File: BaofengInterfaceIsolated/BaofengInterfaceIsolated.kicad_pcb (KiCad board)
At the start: 2 copper layers, 39.4 x 50.8 mm, 11 parts, among them J1 CONN_01X06, J2 CONN_01X02, J3 JACK_TRS_3PINS, J4 JACK_TRS_3PINS, J5 CONN_01X03, J6 CONN_02X04, J7 CONN_01X02, T1 LM-NP-1001-B1L, T2 LM-NP-1001-B1L, U1 LTV-817

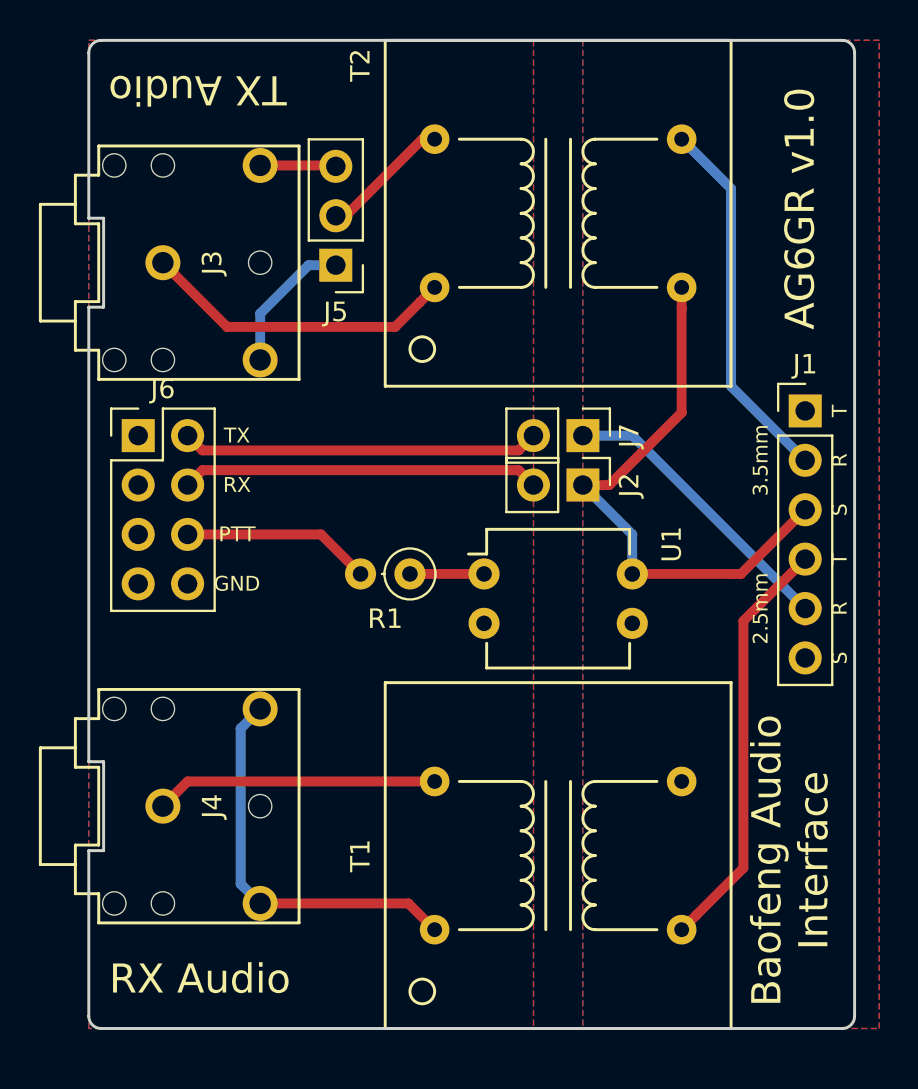
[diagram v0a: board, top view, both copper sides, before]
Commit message: Cleanup board edge, silkscreen
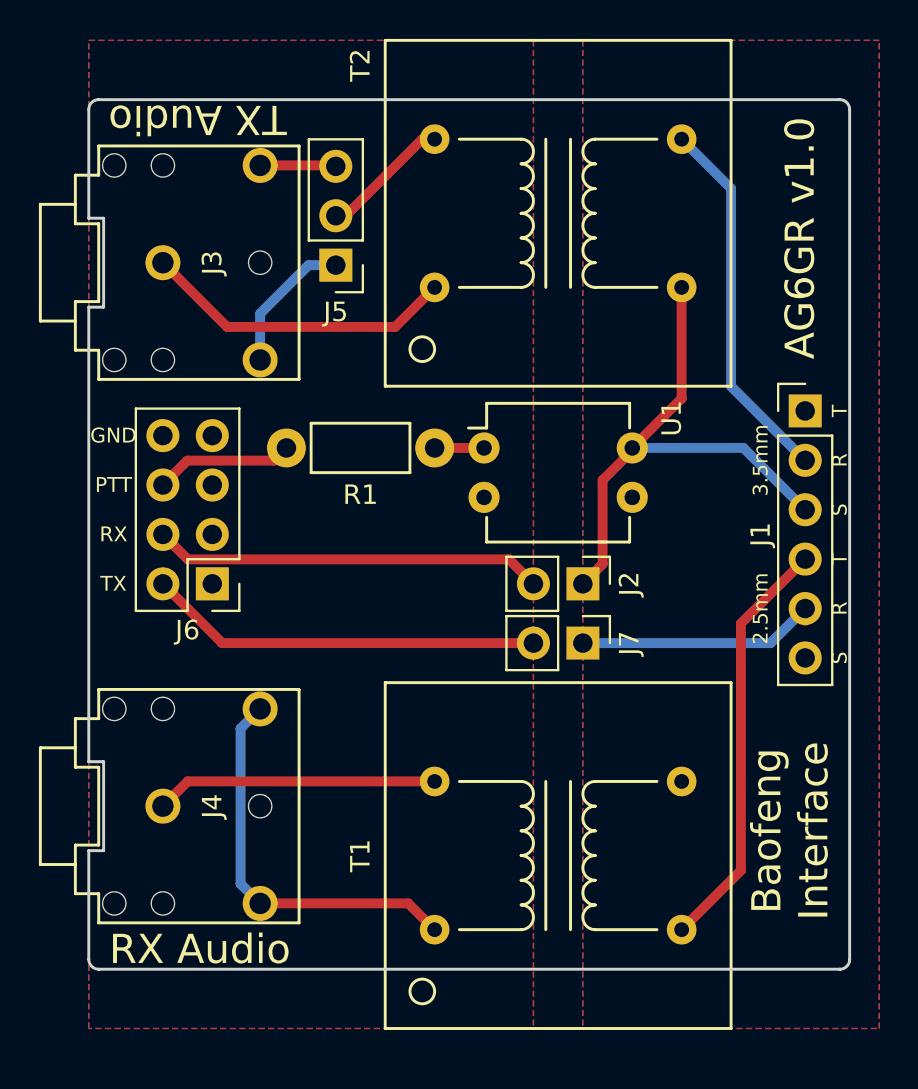
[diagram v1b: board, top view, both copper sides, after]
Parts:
- R1: footprint Resistors_THT:R_Axial_DIN0207_L6.3mm_D2.5mm_P2.54mm_Vertical -> Resistors_THT:Resistor_Horizontal_RM7mm
- moved J7 10.7 mm to (127.0, 132.6)
- moved J6 8.52 mm to (108.0, 129.5), turned to 180 degrees
- moved R1 6.60 mm to (119.4, 122.6)
- moved U1 6.48 mm to (121.9, 122.6)
- moved J2 5.08 mm to (127.0, 129.5)
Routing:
- net Net-(J1-Pad5): track 15.7 -> 12.8 mm
- net PTT_B: track 9.99 -> 7.14 mm
- net SERIAL_TX: track 18.4 -> 20.3 mm
- net SERIAL_RX: track 18.4 -> 20.1 mm
- net TX_AUDIO-: track 28.9 -> 27.5 mm
- net Net-(R1-Pad1): track 3.81 -> 2.72 mm
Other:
- board size 39.4 x 50.8 mm -> 39.1 x 44.7 mm
- board text added: "Baofeng Interface"
- board text removed: "Baofeng Audio Interface"

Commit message: Finish Via Stitching
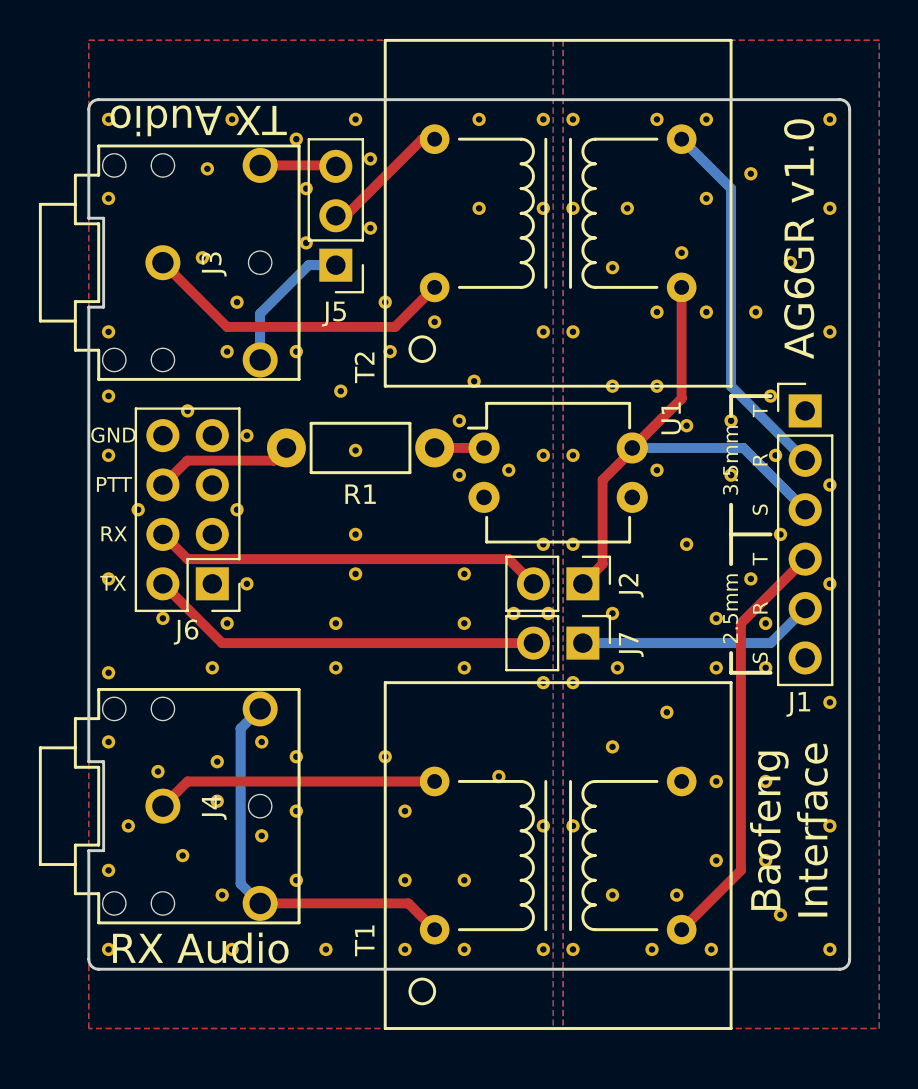
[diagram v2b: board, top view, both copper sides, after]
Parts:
- added REF**: VIA_13_7, Vias:VIA_13_7, F.Cu at (132.3, 121.4)
- added REF**: VIA_13_7, Vias:VIA_13_7, F.Cu at (129.3, 110.2)
- added REF**: VIA_13_7, Vias:VIA_13_7, F.Cu at (109.2, 125.7)
- added REF**: VIA_13_7, Vias:VIA_13_7, F.Cu at (120.7, 124.0)
- added REF**: VIA_13_7, Vias:VIA_13_7, F.Cu at (123.4, 131.1)
- added REF**: VIA_13_7, Vias:VIA_13_7, F.Cu at (120.9, 131.6)
- added REF**: VIA_13_7, Vias:VIA_13_7, F.Cu at (120.9, 129.0)
- added REF**: VIA_13_7, Vias:VIA_13_7, F.Cu at (108.7, 131.6)
- added REF**: VIA_13_7, Vias:VIA_13_7, F.Cu at (109.7, 129.5)
- added REF**: VIA_13_7, Vias:VIA_13_7, F.Cu at (117.9, 144.8)
- added REF**: VIA_13_7, Vias:VIA_13_7, F.Cu at (112.3, 144.8)
- added REF**: VIA_13_7, Vias:VIA_13_7, F.Cu at (117.9, 141.2)
- added REF**: VIA_13_7, Vias:VIA_13_7, F.Cu at (135.6, 129.3)
- added REF**: VIA_13_7, Vias:VIA_13_7, F.Cu at (112.3, 141.2)
- added REF**: VIA_13_7, Vias:VIA_13_7, F.Cu at (102.6, 119.9)
- added REF**: VIA_13_7, Vias:VIA_13_7, F.Cu at (102.6, 144.3)
- added REF**: VIA_13_7, Vias:VIA_13_7, F.Cu at (102.6, 137.7)
- added REF**: VIA_13_7, Vias:VIA_13_7, F.Cu at (102.6, 105.7)
- added REF**: VIA_13_7, Vias:VIA_13_7, F.Cu at (102.6, 109.7)
- added REF**: VIA_13_7, Vias:VIA_13_7, F.Cu at (102.6, 116.6)
- added REF**: VIA_13_7, Vias:VIA_13_7, F.Cu at (102.6, 122.9)
- added REF**: VIA_13_7, Vias:VIA_13_7, F.Cu at (102.6, 129.3)
- added REF**: VIA_13_7, Vias:VIA_13_7, F.Cu at (102.6, 134.1)
- added REF**: VIA_13_7, Vias:VIA_13_7, F.Cu at (132.1, 112.5)
- added REF**: VIA_13_7, Vias:VIA_13_7, F.Cu at (103.6, 142.0)
- added REF**: VIA_13_7, Vias:VIA_13_7, F.Cu at (125.0, 105.7)
- added REF**: VIA_13_7, Vias:VIA_13_7, F.Cu at (125.0, 110.2)
- added REF**: VIA_13_7, Vias:VIA_13_7, F.Cu at (125.0, 116.6)
- added REF**: VIA_13_7, Vias:VIA_13_7, F.Cu at (125.0, 122.9)
- added REF**: VIA_13_7, Vias:VIA_13_7, F.Cu at (125.0, 127.5)
- added REF**: VIA_13_7, Vias:VIA_13_7, F.Cu at (125.0, 134.6)
- added REF**: VIA_13_7, Vias:VIA_13_7, F.Cu at (125.0, 142.0)
- added REF**: VIA_13_7, Vias:VIA_13_7, F.Cu at (117.9, 148.3)
- added REF**: VIA_13_7, Vias:VIA_13_7, F.Cu at (125.0, 148.3)
- added REF**: VIA_13_7, Vias:VIA_13_7, F.Cu at (130.8, 115.6)
- added REF**: VIA_13_7, Vias:VIA_13_7, F.Cu at (120.9, 148.3)
- added REF**: VIA_13_7, Vias:VIA_13_7, F.Cu at (113.8, 148.3)
- added REF**: VIA_13_7, Vias:VIA_13_7, F.Cu at (109.0, 148.3)
- added REF**: VIA_13_7, Vias:VIA_13_7, F.Cu at (102.6, 148.3)
- added REF**: VIA_13_7, Vias:VIA_13_7, F.Cu at (130.8, 119.4)
- added REF**: VIA_13_7, Vias:VIA_13_7, F.Cu at (133.9, 139.7)
- added REF**: VIA_13_7, Vias:VIA_13_7, F.Cu at (136.4, 139.7)
- added REF**: VIA_13_7, Vias:VIA_13_7, F.Cu at (136.4, 143.8)
- added REF**: VIA_13_7, Vias:VIA_13_7, F.Cu at (131.8, 145.5)
- added REF**: VIA_13_7, Vias:VIA_13_7, F.Cu at (133.9, 143.8)
- added REF**: VIA_13_7, Vias:VIA_13_7, F.Cu at (128.5, 113.3)
- added REF**: VIA_13_7, Vias:VIA_13_7, F.Cu at (134.6, 124.0)
- added REF**: VIA_13_7, Vias:VIA_13_7, F.Cu at (137.2, 127.0)
- added REF**: VIA_13_7, Vias:VIA_13_7, F.Cu at (130.6, 148.3)
- added REF**: VIA_13_7, Vias:VIA_13_7, F.Cu at (133.9, 131.3)
- added REF**: VIA_13_7, Vias:VIA_13_7, F.Cu at (133.9, 133.9)
- added REF**: VIA_13_7, Vias:VIA_13_7, F.Cu at (136.4, 131.6)
- added REF**: VIA_13_7, Vias:VIA_13_7, F.Cu at (136.4, 133.9)
- added REF**: VIA_13_7, Vias:VIA_13_7, F.Cu at (128.8, 133.9)
- added REF**: VIA_13_7, Vias:VIA_13_7, F.Cu at (125.2, 131.1)
- added REF**: VIA_13_7, Vias:VIA_13_7, F.Cu at (128.5, 131.1)
- added REF**: VIA_13_7, Vias:VIA_13_7, F.Cu at (137.7, 113.0)
- added REF**: VIA_13_7, Vias:VIA_13_7, F.Cu at (130.8, 123.7)
- added REF**: VIA_13_7, Vias:VIA_13_7, F.Cu at (130.8, 105.7)
- added REF**: VIA_13_7, Vias:VIA_13_7, F.Cu at (135.9, 115.6)
- added REF**: VIA_13_7, Vias:VIA_13_7, F.Cu at (133.3, 115.6)
- added REF**: VIA_13_7, Vias:VIA_13_7, F.Cu at (135.6, 108.5)
- added REF**: VIA_13_7, Vias:VIA_13_7, F.Cu at (133.3, 109.7)
- added REF**: VIA_13_7, Vias:VIA_13_7, F.Cu at (136.7, 119.9)
- added REF**: VIA_13_7, Vias:VIA_13_7, F.Cu at (134.6, 121.2)
- added REF**: VIA_13_7, Vias:VIA_13_7, F.Cu at (136.9, 122.9)
- added REF**: VIA_13_7, Vias:VIA_13_7, F.Cu at (139.7, 110.2)
- added REF**: VIA_13_7, Vias:VIA_13_7, F.Cu at (131.3, 136.1)
- added REF**: VIA_13_7, Vias:VIA_13_7, F.Cu at (139.7, 116.6)
- added REF**: VIA_13_7, Vias:VIA_13_7, F.Cu at (139.7, 124.5)
- added REF**: VIA_13_7, Vias:VIA_13_7, F.Cu at (139.7, 129.5)
- added REF**: VIA_13_7, Vias:VIA_13_7, F.Cu at (139.7, 135.6)
- added REF**: VIA_13_7, Vias:VIA_13_7, F.Cu at (139.7, 142.0)
- added REF**: VIA_13_7, Vias:VIA_13_7, F.Cu at (139.7, 148.3)
- added REF**: VIA_13_7, Vias:VIA_13_7, F.Cu at (133.6, 148.3)
- added REF**: VIA_13_7, Vias:VIA_13_7, F.Cu at (126.5, 148.3)
- added REF**: VIA_13_7, Vias:VIA_13_7, F.Cu at (126.5, 142.0)
- added REF**: VIA_13_7, Vias:VIA_13_7, F.Cu at (126.5, 134.6)
- added REF**: VIA_13_7, Vias:VIA_13_7, F.Cu at (132.3, 127.5)
- added REF**: VIA_13_7, Vias:VIA_13_7, F.Cu at (126.5, 127.5)
- added REF**: VIA_13_7, Vias:VIA_13_7, F.Cu at (126.5, 122.9)
- added REF**: VIA_13_7, Vias:VIA_13_7, F.Cu at (126.5, 116.6)
- added REF**: VIA_13_7, Vias:VIA_13_7, F.Cu at (126.5, 110.2)
- added REF**: VIA_13_7, Vias:VIA_13_7, F.Cu at (126.5, 105.7)
- added REF**: VIA_13_7, Vias:VIA_13_7, F.Cu at (133.3, 105.7)
- added REF**: VIA_13_7, Vias:VIA_13_7, F.Cu at (108.2, 138.7)
- added REF**: VIA_13_7, Vias:VIA_13_7, F.Cu at (108.2, 140.7)
- added REF**: VIA_13_7, Vias:VIA_13_7, F.Cu at (108.5, 145.5)
- added REF**: VIA_13_7, Vias:VIA_13_7, F.Cu at (110.5, 142.5)
- added REF**: VIA_13_7, Vias:VIA_13_7, F.Cu at (137.2, 146.6)
- added REF**: VIA_13_7, Vias:VIA_13_7, F.Cu at (110.5, 137.7)
- added REF**: VIA_13_7, Vias:VIA_13_7, F.Cu at (106.4, 143.5)
- added REF**: VIA_13_7, Vias:VIA_13_7, F.Cu at (107.4, 112.8)
- added REF**: VIA_13_7, Vias:VIA_13_7, F.Cu at (107.7, 108.2)
- added REF**: VIA_13_7, Vias:VIA_13_7, F.Cu at (114.6, 119.6)
- added REF**: VIA_13_7, Vias:VIA_13_7, F.Cu at (120.7, 121.2)
- added REF**: VIA_13_7, Vias:VIA_13_7, F.Cu at (123.2, 123.7)
- added REF**: VIA_13_7, Vias:VIA_13_7, F.Cu at (112.8, 112.0)
- added REF**: VIA_13_7, Vias:VIA_13_7, F.Cu at (105.2, 139.2)
- added REF**: VIA_13_7, Vias:VIA_13_7, F.Cu at (112.3, 138.4)
- added REF**: VIA_13_7, Vias:VIA_13_7, F.Cu at (128.5, 145.5)
- added REF**: VIA_13_7, Vias:VIA_13_7, F.Cu at (116.8, 138.4)
- added REF**: VIA_13_7, Vias:VIA_13_7, F.Cu at (122.7, 139.4)
- added REF**: VIA_13_7, Vias:VIA_13_7, F.Cu at (120.9, 144.8)
- added REF**: VIA_13_7, Vias:VIA_13_7, F.Cu at (115.3, 129.0)
- added REF**: VIA_13_7, Vias:VIA_13_7, F.Cu at (115.3, 122.7)
- added REF**: VIA_13_7, Vias:VIA_13_7, F.Cu at (121.4, 119.1)
- added REF**: VIA_13_7, Vias:VIA_13_7, F.Cu at (121.7, 110.2)
- added REF**: VIA_13_7, Vias:VIA_13_7, F.Cu at (117.1, 117.6)
- added REF**: VIA_13_7, Vias:VIA_13_7, F.Cu at (119.4, 116.1)
- added REF**: VIA_13_7, Vias:VIA_13_7, F.Cu at (139.7, 105.7)
- added REF**: VIA_13_7, Vias:VIA_13_7, F.Cu at (128.5, 137.9)
- added REF**: VIA_13_7, Vias:VIA_13_7, F.Cu at (121.7, 105.7)
- added REF**: VIA_13_7, Vias:VIA_13_7, F.Cu at (115.3, 105.7)
- added REF**: VIA_13_7, Vias:VIA_13_7, F.Cu at (109.0, 105.7)
- added REF**: VIA_13_7, Vias:VIA_13_7, F.Cu at (116.1, 107.7)
- added REF**: VIA_13_7, Vias:VIA_13_7, F.Cu at (112.3, 106.7)
- added REF**: VIA_13_7, Vias:VIA_13_7, F.Cu at (112.8, 109.2)
- added REF**: VIA_13_7, Vias:VIA_13_7, F.Cu at (116.1, 111.3)
- added REF**: VIA_13_7, Vias:VIA_13_7, F.Cu at (109.2, 115.1)
- added REF**: VIA_13_7, Vias:VIA_13_7, F.Cu at (116.8, 115.1)
- added REF**: VIA_13_7, Vias:VIA_13_7, F.Cu at (109.7, 121.9)
- added REF**: VIA_13_7, Vias:VIA_13_7, F.Cu at (128.5, 119.4)
- added REF**: VIA_13_7, Vias:VIA_13_7, F.Cu at (120.9, 133.9)
- added REF**: VIA_13_7, Vias:VIA_13_7, F.Cu at (114.3, 131.6)
- added REF**: VIA_13_7, Vias:VIA_13_7, F.Cu at (114.3, 133.9)
- added REF**: VIA_13_7, Vias:VIA_13_7, F.Cu at (108.0, 133.9)
- added REF**: VIA_13_7, Vias:VIA_13_7, F.Cu at (105.4, 131.3)
- added REF**: VIA_13_7, Vias:VIA_13_7, F.Cu at (104.1, 125.7)
- added REF**: VIA_13_7, Vias:VIA_13_7, F.Cu at (106.7, 120.7)
- added REF**: VIA_13_7, Vias:VIA_13_7, F.Cu at (108.7, 117.6)
- added REF**: VIA_13_7, Vias:VIA_13_7, F.Cu at (112.3, 117.6)
- added REF**: VIA_13_7, Vias:VIA_13_7, F.Cu at (115.3, 127.0)
